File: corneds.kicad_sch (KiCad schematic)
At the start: 124 parts, among them J3 AudioJack4, J4 AudioJack4, SW1 SW_Push, SW10 SW_Push, SW11 SW_Push, SW12 SW_Push, SW13 SW_Push, SW14 SW_Push, SW15 SW_Push, SW16 SW_Push, SW17 SW_Push, SW18 SW_Push, SW19 SW_Push, SW2 SW_Push, SW20 SW_Push, SW21 SW_Push, SW22 SW_Push, SW23 SW_Push, SW24 SW_Push, SW25 SW_Push, SW26 SW_Push, SW27 SW_Push, SW28 SW_Push, SW29 SW_Push, SW3 SW_Push, SW30 SW_Push, SW31 SW_Push, SW32 SW_Push, SW33 SW_Push, SW34 SW_Push, SW35 SW_Push, SW36 SW_Push, SW37 SW_Push, SW38 SW_Push, SW39 SW_Push, SW4 SW_Push, SW40 SW_Push, SW41 SW_Push, SW42 SW_Push, SW5 SW_Push, SW6 SW_Push, SW7 SW_Push, SW8 SW_Push, SW9 SW_Push, U1 Pico, U2 Pico, U3 SWD_Connector_3pin, U4 SWD_Connector_3pin, U5 Debug_UART_l, U6 Debug_UART_r

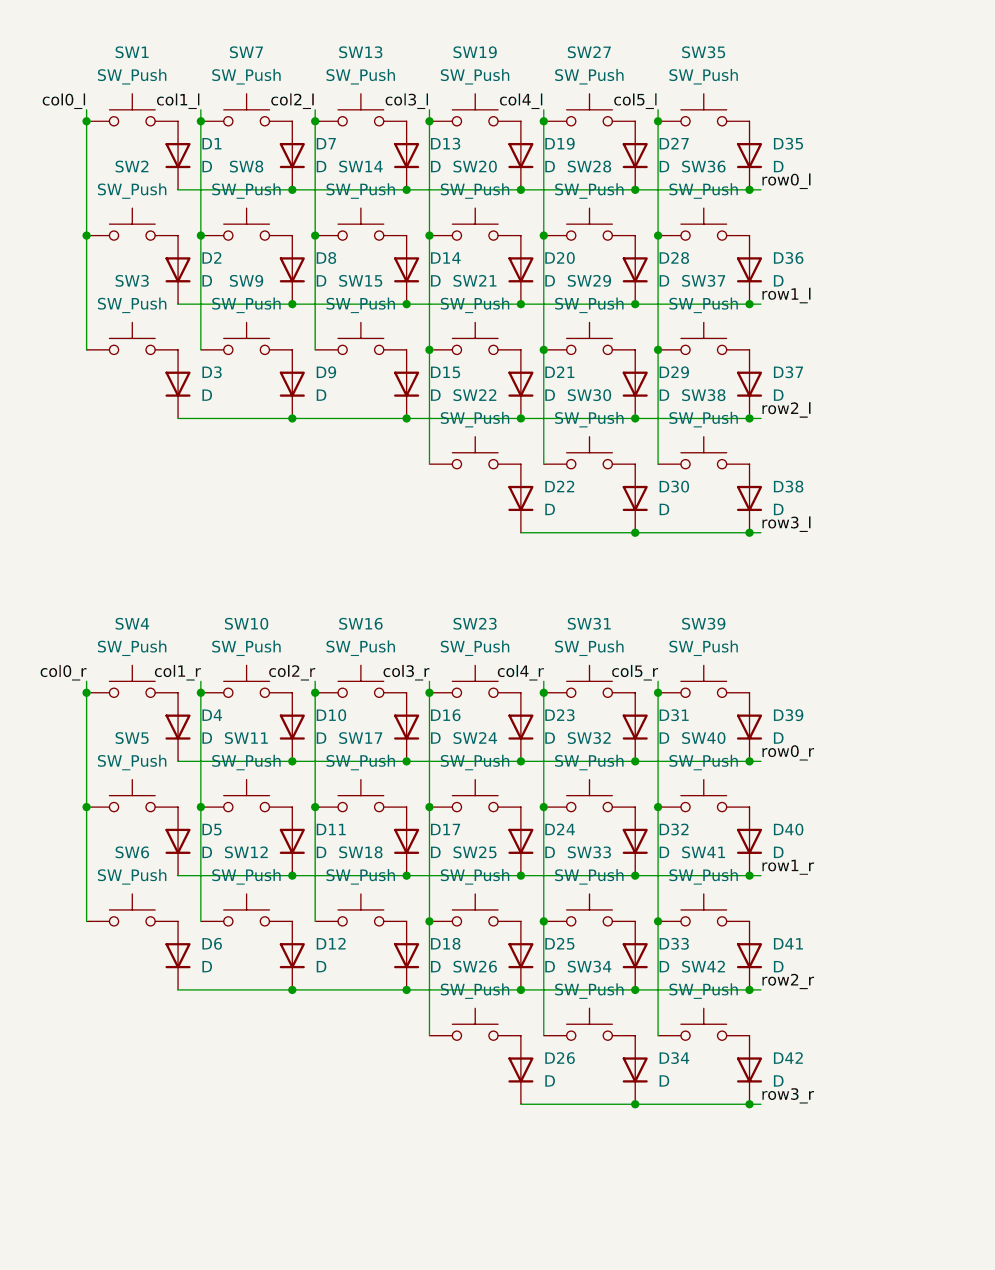
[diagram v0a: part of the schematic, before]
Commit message: removed cols and rows on key switches in sch
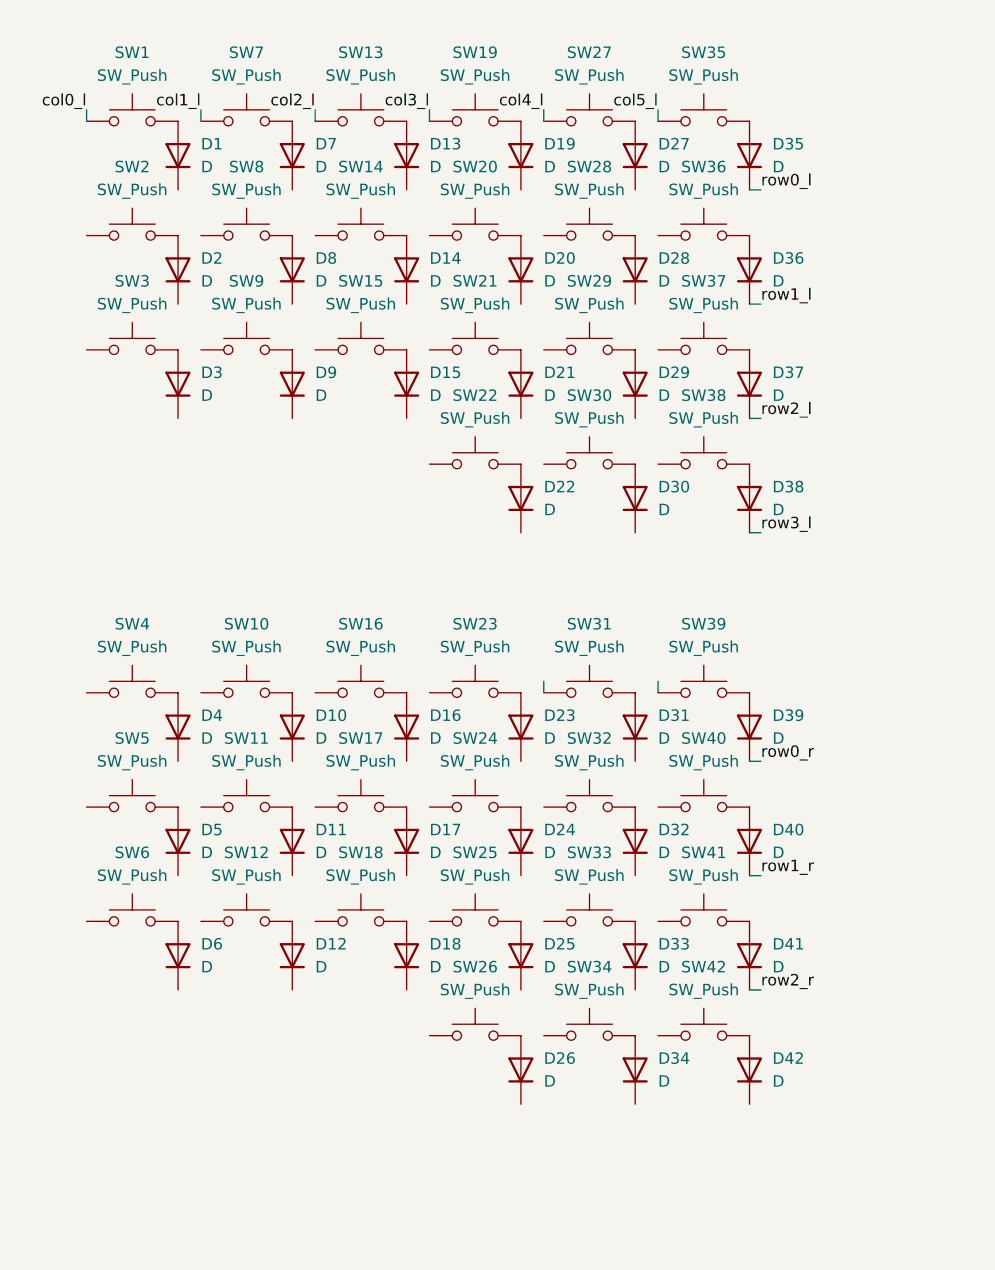
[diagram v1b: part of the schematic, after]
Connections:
- net col0_l: no longer SW2.1, SW3.1
- net col0_r: no longer SW4.1, SW5.1, SW6.1
- net col1_l: no longer SW8.1, SW9.1
- net col1_r: no longer SW10.1, SW11.1, SW12.1
- net col2_l: no longer SW14.1, SW15.1
- net col2_r: no longer SW16.1, SW17.1, SW18.1
- net col3_l: no longer SW20.1, SW21.1, SW22.1
- net col3_r: no longer SW23.1, SW24.1, SW25.1, SW26.1
- net col4_l: no longer SW28.1, SW29.1, SW30.1
- net col4_r: no longer SW31.1, SW32.1, SW33.1, SW34.1
- net col5_l: no longer SW36.1, SW37.1, SW38.1
- net col5_r: no longer SW39.1, SW40.1, SW41.1, SW42.1
- net row0_l: no longer D1.1 (K), D13.1 (K), D19.1 (K), D27.1 (K), D7.1 (K)
- net row0_r: no longer D10.1 (K), D16.1 (K), D23.1 (K), D31.1 (K), D4.1 (K)
- net row1_l: no longer D14.1 (K), D2.1 (K), D20.1 (K), D28.1 (K), D8.1 (K)
- net row1_r: no longer D11.1 (K), D17.1 (K), D24.1 (K), D32.1 (K), D5.1 (K)
- net row2_l: no longer D15.1 (K), D21.1 (K), D29.1 (K), D3.1 (K), D9.1 (K)
- net row2_r: no longer D12.1 (K), D18.1 (K), D25.1 (K), D33.1 (K), D6.1 (K)
- net row3_l: no longer D22.1 (K), D30.1 (K)
- net row3_r: no longer D26.1 (K), D34.1 (K), D42.1 (K)
